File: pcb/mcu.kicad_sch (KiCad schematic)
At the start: 29 parts, among them J1 SWD+UART, SW1 BOOT, SW2 RESET, SW3 USER, U1 RP2350A, U2 W25Q128JVS, Y1 12MHz

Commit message: specify the magnetics and the crystals by what they have to do
Each inductor now states the current it has to stay unsaturated to, derived rather than copied: the
processor's own datasheet fixes 1.5A for the core regulator, the charger's output side carries
about 6.3A when the input is delivering its full 27W into a system near 4V, and each of the two
converters wants an inductor that holds up past its own current limit so the part protects itself
before the magnetics give up. The crystals state a load capacitance, which is the number that
actually decides whether they oscillate on frequency.

Two things came out of reading rather than assuming.

The charger's inductor value is not a choice. Its datasheet is explicit that 1.5MHz works only with
1uH and 750kHz only with 2.2uH, and the frequency was already fixed at power-on by the resistor
that also sets the cell count. That resistor therefore picks the inductor, and the two have to move
together or not at all. They are consistent as drawn; the coupling is now written down so they stay
that way.

The core regulator's inductor has to be fully shielded and marked for polarity, and oriented as the
vendor's layout shows, because stray field from it couples into the regulator's control loop and
moves the output even with nominally shielded parts. That is a placement constraint arriving from a
component datasheet, and it is recorded where layout will look for it rather than left in a PDF.

The processor's crystal wants a 10pF load, which the 15pF pair either side of it meets once a
couple of picofarads of stray are allowed. The hub's pair implies about 12pF by the same
arithmetic, and that one stays open: its datasheet and design checklist are both scanned images,
so nothing reads out of them without rendering the pages.

Co-Authored-By: Claude Opus 5 (1M context) <noreply@anthropic.com>
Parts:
- FB1: Current (none) -> 100mA; Tolerance (none) -> 25%
- L1: Isat (none) -> 1.5A; Shielding (none) -> fully shielded, polarity marked; Tolerance (none) -> 20%
- Y1: Load (none) -> 10pF; Tolerance (none) -> 30ppm
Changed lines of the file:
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@@
+			)
+		)
+		(property "Tolerance" "20%"
+			(at 208.28 91.44 0)
+			(show_name no)
+			(do_not_autoplace no)
+			(effects
+				(font
+					(size 1.27 1.27)
+				)
+				(hide yes)
+			)
+		)
+		(property "Isat" "1.5A"
+			(at 208.28 91.44 0)
+			(show_name no)
+			(do_not_autoplace no)
+			(effects
+				(font
+					(size 1.27 1.27)
+				)
+				(hide yes)
+			)
+		)
+		(property "Shielding" "fully shielded, polarity marked"
+			(at 208.28 91.44 0)
+			(show_name no)
+			(do_not_autoplace no)
+			(effects
+				(font
+					(size 1.27 1.27)
+				)
+				(hide yes)
 			)
 		)
@@
 			)
 		)
+		(property "Tolerance" "25%"
+			(at 189.23 60.96 0)
+			(show_name no)
+			(do_not_autoplace no)
+			(effects
+				(font
+					(size 1.27 1.27)
+				)
+				(hide yes)
+			)
+		)
+		(property "Current" "100mA"
+			(at 189.23 60.96 0)
+			(show_name no)
+			(do_not_autoplace no)
+			(effects
+				(font
+					(size 1.27 1.27)
+				)
+				(hide yes)
+			)
+		)
 		(property "Footprint" ""
 			(at 189.23 53.34 0)
@@
 			)
 		)
+		(property "Tolerance" "30ppm"
+			(at 147.32 172.72 0)
+			(show_name no)
+			(do_not_autoplace no)
+			(effects
+				(font
+					(size 1.27 1.27)
+				)
+				(hide yes)
+			)
+		)
+		(property "Load" "10pF"
+			(at 147.32 172.72 0)
+			(show_name no)
+			(do_not_autoplace no)
+			(effects
+				(font
+					(size 1.27 1.27)
+				)
+				(hide yes)
+			)
+		)

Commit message: choose the indicators and buttons, and let the resistor pick the colour
The indicators run from a 3.3V pin through 1k, so the current is decided entirely by forward
voltage: about 1.3mA for red, amber or ordinary green, and about 0.3mA for true green, blue or
white, which is not enough to rely on seeing. The low-voltage colours are not a preference here,
they are a requirement of the resistor already drawn. Taken as red and green, and the document says
why so that fitting a blue one later is a visible decision rather than a surprise. 1.3mA is modest
on purpose: clearly visible indoors on a modern part, and two left on cost the cell about a
fiftieth of its capacity a day.

The three buttons are one part, surface mount, top-actuated, at the edge: one line item, an
actuator big enough to press on a bare board, and an enclosure that wants a hole rather than a
plunger. Two things recorded for whoever draws that enclosure. Only the user button is one an owner
should reach, since the other two enter the bootloader and reset the board, so recessing them is
reasonable even though all three share an edge. And the user button has no pull-up on the board --
it relies on the processor's internal one, which is ordinary, but it means the pin floats until
firmware configures it.

Co-Authored-By: Claude Opus 5 (1M context) <noreply@anthropic.com>
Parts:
- D1: value LED -> red
- D2: value LED -> green
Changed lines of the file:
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@@
 			)
 		)
-		(property "Value" "LED"
+		(property "Value" "red"
 			(at 273.05 163.068 0)
 			(show_name no)
@@
 			)
 		)
-		(property "Value" "LED"
+		(property "Value" "green"
 			(at 261.874 176.022 0)
 			(show_name no)

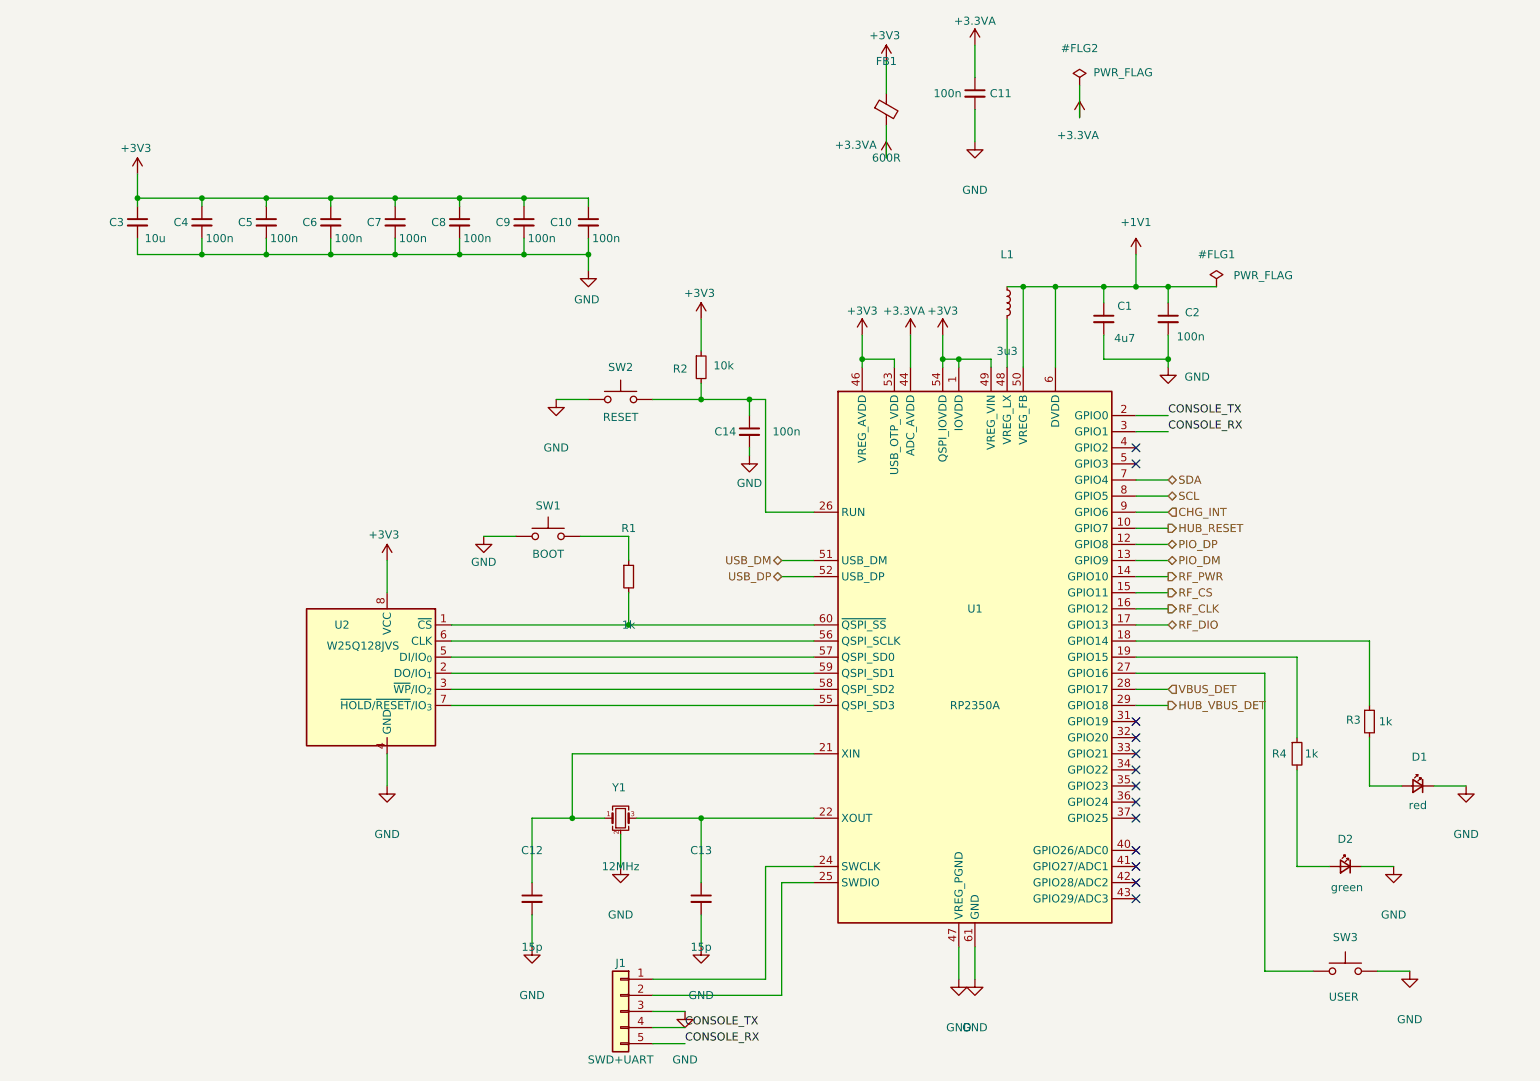
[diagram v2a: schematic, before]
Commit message: calculate the capacitor banks, and give every one of them a package
The question a value and a rating leave open is how much capacitance is actually there once the
voltage is across it, and the answer differs by package for the same value and rating. So the
requirement is derived bank by bank rather than taken from the vendors' part counts.

The charger's input is the binding case. Holding its input ripple to 100 mV with 5.4 A through the
inductor needs 8.6uF in circuit out of the 20uF fitted, so 43% has to survive 9V. The 5V rail needs
36% of what it carries and the system rail 27%. That last one is worth stating properly: ripple
alone would want only 2.5uF there, so the bank exists to answer load steps, and the realistic fast
step is the radio transmitting and the processor waking rather than the ports, which cannot step
quickly because the boost soft-starts over 4ms. At half an amp over five microseconds that is 25uF
against about 70uF effective.

43% is comfortable in 1206 and marginal in 0603 for a 10uF part at 9V, so the five capacitors on
the 9V nodes take 1206 and everything at 4.5V or under takes 0805. Decoupling goes to 0402, where
being near the pin matters more than the package, and the frequency- and loop-setting parts to
0603, where there is nothing to derate.

The answer to the open item is that the counts do not change: every bank is adequate as drawn
provided each part keeps roughly half of itself, which is what the package choice delivers. What is
left is a purchasing check rather than a design one.

Two asymmetries recorded. The 3.3V converter's vendor states that its recommended values anticipate
tolerance and bias derating and quotes 20% and 50%, so its table is nominal with the margin already
in it; the charger's and the boost's say nothing, so there the derating is ours to carry. And the
processor specifies an effective tolerance rather than a nominal one -- its core regulator's output
capacitor must be 4.7uF +/-20% in circuit.

The checker's 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
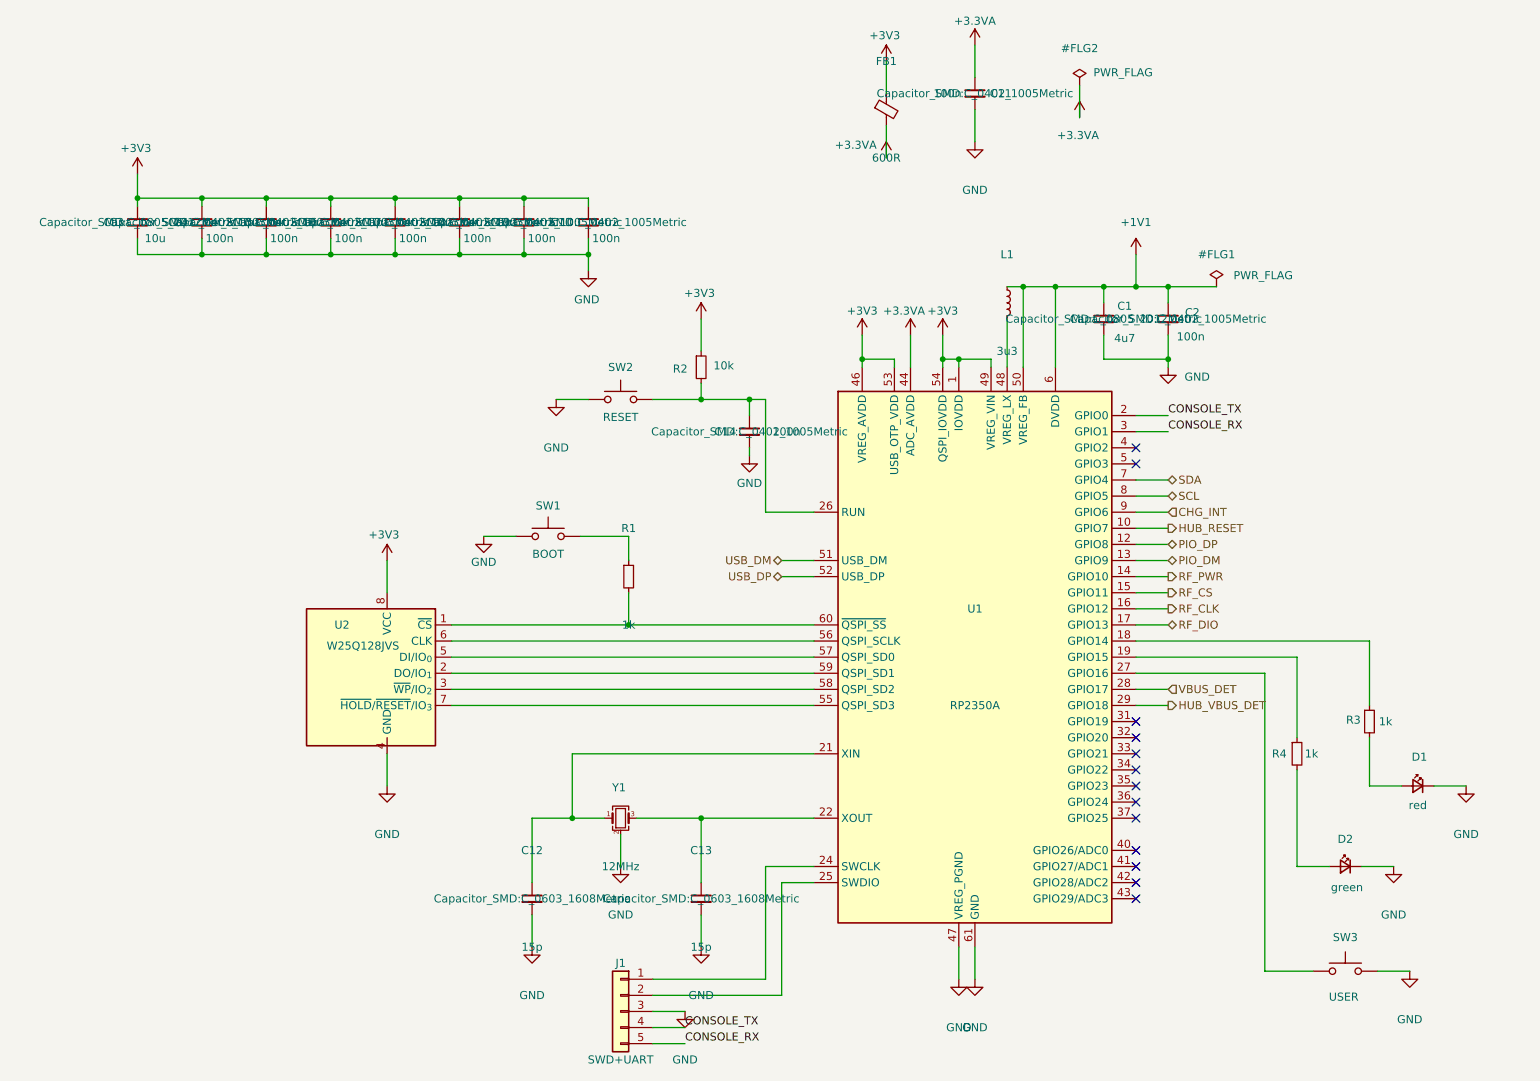
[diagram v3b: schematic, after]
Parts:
- C1, C3: footprint (none) -> Capacitor_SMD:C_0805_2012Metric
- C10, C11, C14, C2, C4, C5, C6, C7, C8, C9: footprint (none) -> Capacitor_SMD:C_0402_1005Metric
- C12, C13: footprint (none) -> Capacitor_SMD:C_0603_1608Metric
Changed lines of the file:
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@@
 			)
 		)
-		(property "Footprint" ""
+		(property "Footprint" "Capacitor_SMD:C_0402_1005Metric"
 			(at 121.92 71.12 0)
 			(show_name no)
@@
 			)
 		)
-		(property "Footprint" ""
+		(property "Footprint" "Capacitor_SMD:C_0402_1005Metric"
 			(at 91.44 71.12 0)
 			(show_name no)
@@
 			)
 		)
-		(property "Footprint" ""
+		(property "Footprint" "Capacitor_SMD:C_0402_1005Metric"
 			(at 142.24 71.12 0)
 			(show_name no)
@@
 			)
 		)
-		(property "Footprint" ""
+		(property "Footprint" "Capacitor_SMD:C_0402_1005Metric"
 			(at 132.08 71.12 0)
 			(show_name no)
@@
 			)
 		)
-		(property "Footprint" ""
+		(property "Footprint" "Capacitor_SMD:C_0402_1005Metric"
 			(at 111.76 71.12 0)
 			(show_name no)
@@
 			)
 		)
-		(property "Footprint" ""
+		(property "Footprint" "Capacitor_SMD:C_0603_1608Metric"
 			(at 160.02 177.8 0)
 			(show_name no)
@@
 			)
 		)
-		(property "Footprint" ""
+		(property "Footprint" "Capacitor_SMD:C_0402_1005Metric"
 			(at 203.2 50.8 0)
 			(show_name no)
@@
 			)
 		)
-		(property "Footprint" ""
+		(property "Footprint" "Capacitor_SMD:C_0603_1608Metric"
 			(at 133.35 177.8 0)
 			(show_name no)
@@
 			)
 		)
-		(property "Footprint" ""
+		(property "Footprint" "Capacitor_SMD:C_0805_2012Metric"
 			(at 223.52 86.36 0)
 			(show_name no)
@@
 			)
 		)
-		(property "Footprint" ""
+		(property "Footprint" "Capacitor_SMD:C_0402_1005Metric"
 			(at 101.6 71.12 0)
 			(show_name no)
@@
 			)
 		)
-		(property "Footprint" ""
+		(property "Footprint" "Capacitor_SMD:C_0805_2012Metric"
 			(at 71.12 71.12 0)
 			(show_name no)
@@
 			)
 		)
-		(property "Footprint" ""
+		(property "Footprint" "Capacitor_SMD:C_0402_1005Metric"
 			(at 167.64 104.14 0)
 			(show_name no)
@@
 			)
 		)
-		(property "Footprint" ""
+		(property "Footprint" "Capacitor_SMD:C_0402_1005Metric"
 			(at 81.28 71.12 0)
 			(show_name no)
@@
 			)
 		)
-		(property "Footprint" ""
+		(property "Footprint" "Capacitor_SMD:C_0402_1005Metric"
 			(at 233.68 86.36 0)
 			(show_name no)
